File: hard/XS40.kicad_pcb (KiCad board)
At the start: 2 copper layers, 160 x 110 mm, 94 parts, among them J1 USB_B_Micro, J2 Conn_01x20_Female, J3 Nu-link, SW1 SW_Push, SW10 SW_Push, SW11 SW_Push, SW12 SW_Push, SW13 SW_Push, SW14 SW_Push, SW15 SW_Push, SW16 SW_Push, SW17 SW_Push, SW18 SW_Push, SW19 SW_Push, SW2 SW_Push, SW20 SW_Push, SW21 SW_Push, SW22 SW_Push, SW23 SW_Push, SW24 SW_Push, SW25 SW_Push, SW26 SW_Push, SW27 SW_Push, SW28 SW_Push, SW29 SW_Push, SW3 SW_Push, SW30 SW_Push, SW31 SW_Push, SW32 SW_Push, SW33 SW_Push, SW34 SW_Push, SW35 SW_Push, SW36 SW_Push, SW37 SW_Push, SW38 SW_Push, SW39 SW_Push, SW4 SW_Push, SW40 SW_Push, SW5 SW_Push, SW6 SW_Push, SW7 SW_Push, SW8 SW_Push, SW9 SW_Push, U1 N76E003AT20, U2 CH9328

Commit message: 更新PCB图
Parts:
- moved C3 114.6 mm to (34.8, 45.4)
- moved J3 105.5 mm to (37.4, 42.0), turned to 270 degrees
- moved C2 97.2 mm to (164.6, 54.4), turned to 0 degrees
- moved C1 88.1 mm to (164.6, 55.9), turned to 180 degrees
- moved D41 83.4 mm to (156.5, 54.7), turned to 0 degrees
- moved D42 74.1 mm to (151.4, 54.7), turned to 180 degrees
- moved JP1 73.5 mm to (142.5, 45.0), turned to 270 degrees
- moved JP2 39.4 mm to (148.1, 45.0), turned to 270 degrees
- moved J2 31.3 mm to (115.7, 44.4), turned to 90 degrees
- moved JP3 27.8 mm to (131.5, 45.0), turned to 270 degrees
- moved JP4 23.9 mm to (137.0, 45.0), turned to 270 degrees
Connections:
- J3 pad 1: VDD -> GND
- J3 pad 2: COL7 -> /RST
- J3 pad 4: /RST -> COL7
- J3 pad 5: GND -> VDD
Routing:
- net COL8: track 0.00 -> 335.6 mm, vias 0 -> 1
- net COL7: track 0.00 -> 304.7 mm, vias 0 -> 2
- net ROW5: track 94.7 -> 383.6 mm, vias 0 -> 4
- net COL6: track 0.00 -> 262.4 mm, vias 0 -> 1
- net ROW4: track 75.5 -> 332.2 mm, vias 0 -> 2
- net COL5: track 0.00 -> 223.6 mm, vias 0 -> 1
- net ROW3: track 56.4 -> 268.0 mm, vias 0 -> 2
- net ROW2: track 37.2 -> 235.2 mm, vias 0 -> 2
- net COL4: track 0.00 -> 185.2 mm, vias 0 -> 1
- net ROW1: track 15.5 -> 192.0 mm, vias 0 -> 1
- net VDD: track 0.00 -> 167.4 mm, vias 0 -> 1
- net COL3: track 0.00 -> 155.7 mm, vias 0 -> 1
- net COL2: track 0.00 -> 151.7 mm, vias 0 -> 1
- net TXD: track 0.00 -> 135.9 mm, vias 0 -> 2
- net RXD: track 0.00 -> 132.5 mm, vias 0 -> 2
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- added copper zone on B.Cu, net GND
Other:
- board text added: "C"
- board text added: "D"
- board text added: "G"
- board text added: "R"
- board text added: "V"

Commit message: PCB定稿；生成Gerber。
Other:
- board text added: "C1"
- board text added: "C2"
- board text added: "C3"
- board text added: "C4"
- board text added: "C5"
- board text added: "C6"
- board text added: "C7"
- board text added: "C8"
- board text added: "GND"
- board text added: "IO1"
- board text added: "P05"
- board text added: "P30"
- board text added: "R1"
- board text added: "R2"
- board text added: "R3"
- board text added: "R4"
- board text added: "R5"
- board text added: "U+"
- board text added: "U-"
- board text added: "V0.1 20200315"
- board text added: "VDD"
- board text added: "XS40"

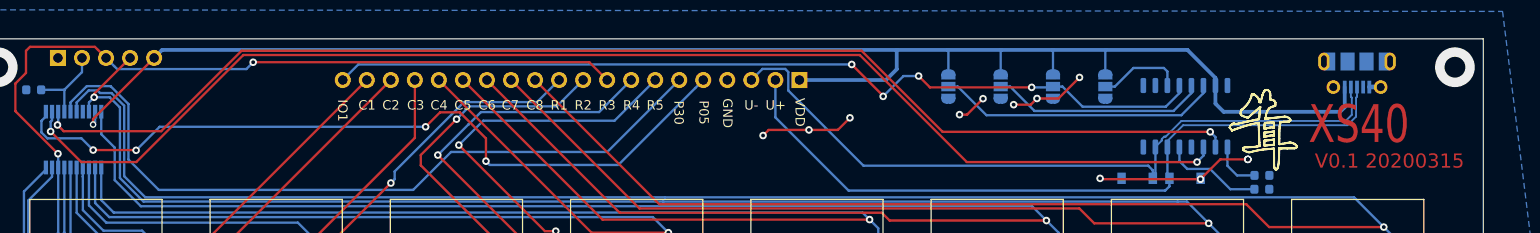
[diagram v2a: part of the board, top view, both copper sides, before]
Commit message: PCB添加了少的一根GND线，打包存档v0.1
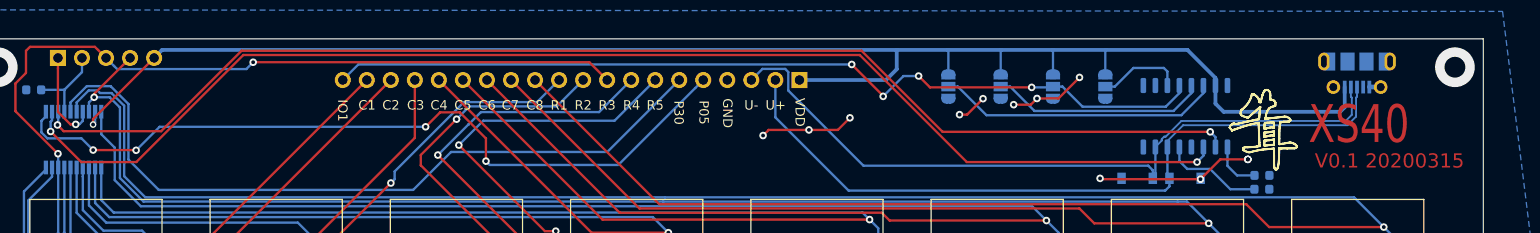
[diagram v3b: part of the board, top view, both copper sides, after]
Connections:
- U1 pad 7: Net-(U1-Pad7) -> GND
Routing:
- net GND: track 39.0 -> 49.0 mm, vias 12 -> 13
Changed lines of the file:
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@@
   (general
     (thickness 1.6)
-    (drawings 562)
-    (tracks 502)
+    (drawings 564)
+    (tracks 510)
     (zones 0)
     (modules 94)
-    (nets 75)
+    (nets 74)
   )
   (page A4)
@@
       (usegerberadvancedattributes false)
       (creategerberjobfile false)
+      (gerberprecision 5)
       (excludeedgelayer true)
       (linewidth 0.100000)
@@
   (net 68 TXD)
   (net 69 RXD)
-  (net 70 "Net-(U1-Pad7)")
-  (net 71 "Net-(U2-Pad4)")
-  (net 72 "Net-(U2-Pad9)")
-  (net 73 "Net-(U2-Pad10)")
-  (net 74 "Net-(U2-Pad16)")
+  (net 70 "Net-(U2-Pad4)")
+  (net 71 "Net-(U2-Pad9)")
+  (net 72 "Net-(U2-Pad10)")
+  (net 73 "Net-(U2-Pad16)")
   (net_class Default 这是默认网络类。
     (clearance 0.2)
@@
     (add_net "Net-(D9-Pad1)")
     (add_net "Net-(J1-Pad4)")
-    (add_net "Net-(U1-Pad7)")
     (add_net "Net-(U2-Pad10)")
     (add_net "Net-(U2-Pad16)")
@@
       (net 20 COL8))
     (pad 7 smd rect (at -2.95 -0.975 270) (size 1.45 0.45) (layers B.Cu B.Paste B.Mask)
-      (net 70 "Net-(U1-Pad7)"))
+      (net 1 GND))
     (pad 8 smd rect (at -2.95 -1.625 270) (size 1.45 0.45) (layers B.Cu B.Paste B.Mask)
       (net 18 COL7))
@@
       (net 68 TXD))
     (pad 4 smd roundrect (at -3.25 0.635 90) (size 1.6 0.6) (layers B.Cu B.Paste B.Mask) (roundrect_rratio 0.25)
-      (net 71 "Net-(U2-Pad4)"))
+      (net 70 "Net-(U2-Pad4)"))
     (pad 5 smd roundrect (at -3.25 -0.635 90) (size 1.6 0.6) (layers B.Cu B.Paste B.Mask) (roundrect_rratio 0.25)
       (net 2 "Net-(C1-Pad2)"))
@@
       (net 1 GND))
     (pad 9 smd roundrect (at 3.25 -4.445 90) (size 1.6 0.6) (layers B.Cu B.Paste B.Mask) (roundrect_rratio 0.25)
-      (net 72 "Net-(U2-Pad9)"))
+      (net 71 "Net-(U2-Pad9)"))
     (pad 10 smd roundrect (at 3.25 -3.175 90) (size 1.6 0.6) (layers B.Cu B.Paste B.Mask) (roundrect_rratio 0.25)
-      (net 73 "Net-(U2-Pad10)"))
+      (net 72 "Net-(U2-Pad10)"))
     (pad 11 smd roundrect (at 3.25 -1.905 90) (size 1.6 0.6) (layers B.Cu B.Paste B.Mask) (roundrect_rratio 0.25)
       (net 65 IO2))
@@
       (net 55 VDD))
     (pad 16 smd roundrect (at 3.25 4.445 90) (size 1.6 0.6) (layers B.Cu B.Paste B.Mask) (roundrect_rratio 0.25)
-      (net 74 "Net-(U2-Pad16)"))
+      (net 73 "Net-(U2-Pad16)"))
     (model ${KISYS3DMOD}/Package_SO.3dshapes/SOP-16_4.55x10.3mm_P1.27mm.wrl
       (at (xyz 0 0 0))
@@
     )
   )
+  (gr_text "V0.1 20200315" (at 178.07432 52.91836) (layer F.Mask)
+    (effects (font (size 1.5 1.5) (thickness 0.26)))
+  )
+  (gr_text XS40 (at 174.84344 49.05248) (layer F.Mask)
+    (effects (font (size 4 3) (thickness 0.65)))
+  )
   (gr_text VDD (at 115.76812 47.761471 270) (layer F.SilkS)
     (effects (font (size 1 1) (thickness 0.15)))
@@
     (effects (font (size 1 1) (thickness 0.15)))
   )
-  (gr_text "V0.1 20200315" (at 178.08956 52.91836) (layer F.Cu)
+  (gr_text "V0.1 20200315" (at 178.08448 52.9082) (layer F.Cu)
     (effects (font (size 1.5 1.5) (thickness 0.2)))
   )
@@
   (segment (start 140.82776 46.3042) (end 143.09852 46.3042) (width 0.25) (layer F.Cu) (net 1))
   (segment (start 143.09852 46.3042) (end 145.32356 44.07916) (width 0.25) (layer F.Cu) (net 1))
+  (segment (start 39.62332 49.03868) (end 39.243 49.03868) (width 0.25) (layer B.Cu) (net 1))
+  (via (at 39.243 49.03868) (size 0.8) (drill 0.4) (layers F.Cu B.Cu) (net 1))
+  (segment (start 39.9894 47.6976) (end 39.9894 48.6726) (width 0.25) (layer B.Cu) (net 1))
+  (segment (start 39.9894 48.6726) (end 39.62332 49.03868) (width 0.25) (layer B.Cu) (net 1))
+  (segment (start 37.3634 43.12176) (end 37.3634 42.02176) (width 0.25) (layer F.Cu) (net 1))
+  (segment (start 37.3634 47.724765) (end 37.3634 43.12176) (width 0.25) (layer F.Cu) (net 1))
+  (segment (start 38.677315 49.03868) (end 37.3634 47.724765) (width 0.25) (layer F.Cu) (net 1))
+  (segment (start 39.243 49.03868) (end 38.677315 49.03868) (width 0.25) (layer F.Cu) (net 1))
   (segment (start 156.706401 53.750041) (end 155.8798 52.92344) (width 0.25) (layer B.Cu) (net 2))
   (segment (start 159.117199 53.750041) (end 156.706401 53.750041) (width 0.25) (layer B.Cu) (net 2))
